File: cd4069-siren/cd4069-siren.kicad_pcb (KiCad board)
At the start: 2 copper layers, 15 parts, among them U1 4069

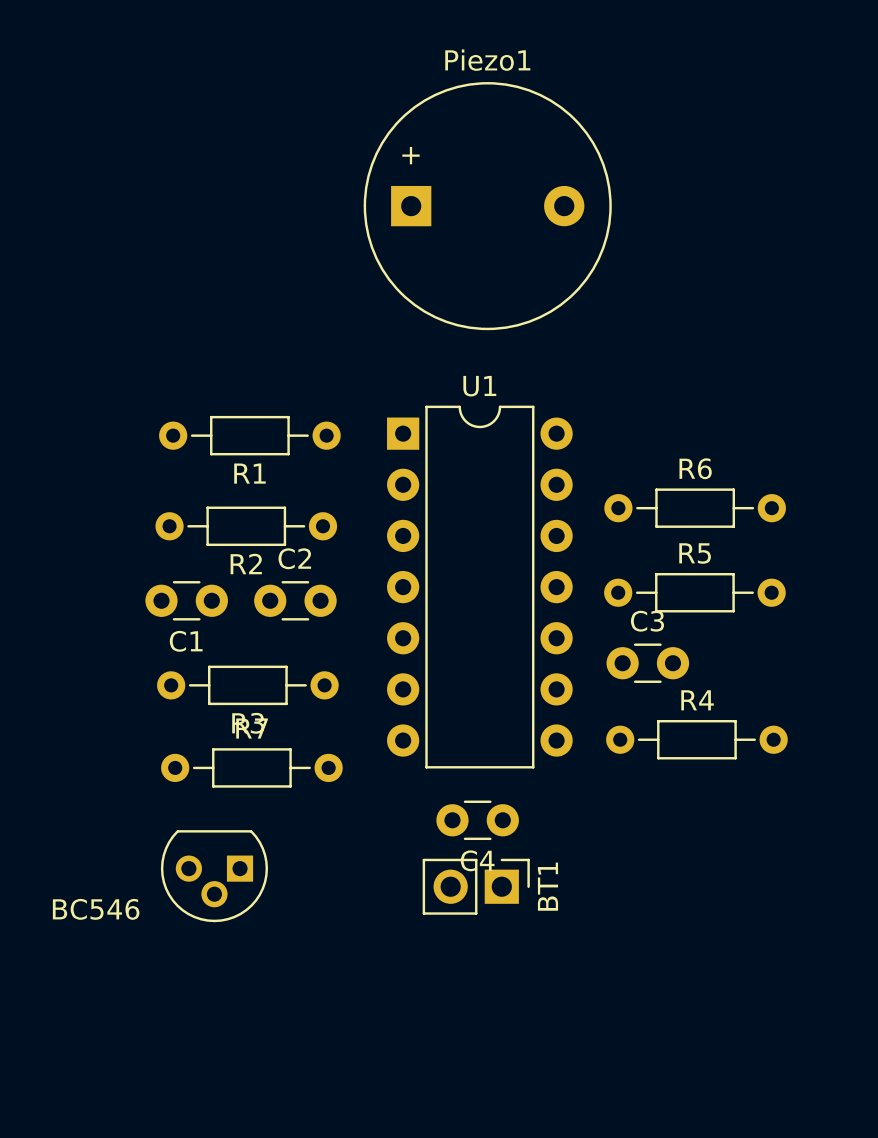
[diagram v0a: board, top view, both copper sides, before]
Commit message: project 7 / cd4069 siren / changed edge cuts, improved tracks, added logo
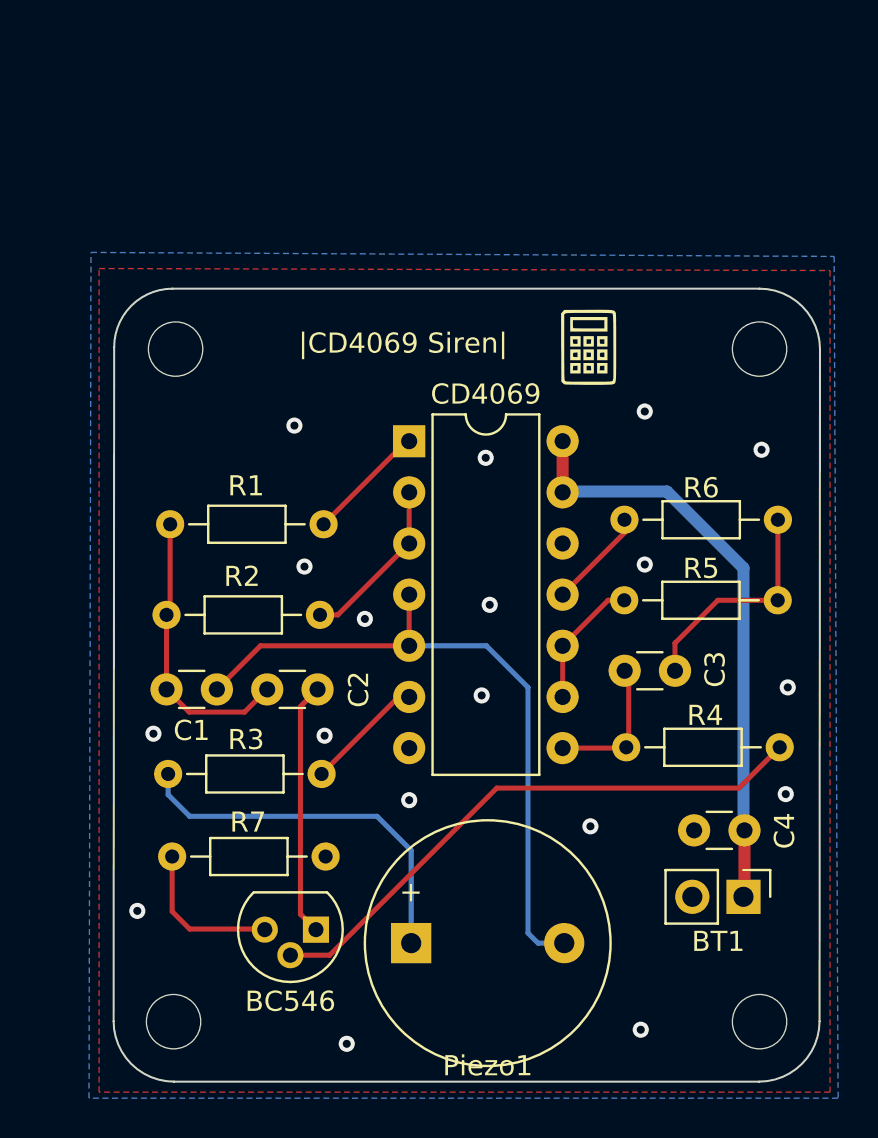
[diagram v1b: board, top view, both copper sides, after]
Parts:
- added G***: LOGO, Graphics:pcbLogo_4mmx4mm, F.Cu at (112.5, 50.3)
- added G***: LOGO, Graphics:pcbLogo_30mmx30mm, B.Cu at (105.9, 68.2)
- added REF**: MountingHole_2.7mm, MountingHole:MountingHole_2.7mm, F.Cu at (121.0, 50.4)
- added REF**: MountingHole_2.7mm, MountingHole:MountingHole_2.7mm, F.Cu at (121.0, 83.8)
- added REF**: MountingHole_2.7mm, MountingHole:MountingHole_2.7mm, F.Cu at (92.0, 50.4)
- added REF**: MountingHole_2.7mm, MountingHole:MountingHole_2.7mm, F.Cu at (91.9, 83.8)
- moved Piezo1 36.6 mm to (103.7, 79.9)
- moved BT1 12.0 mm to (120.2, 77.6)
- moved C4 12.0 mm to (120.2, 74.3)
- moved BC546 4.84 mm to (99.0, 79.2)
- moved C1 4.41 mm to (94.0, 67.3)
- moved R3 4.40 mm to (99.2, 71.5)
- moved C2 4.40 mm to (96.5, 67.3)
- moved R1 4.40 mm to (99.3, 59.1)
- moved R2 4.40 mm to (99.2, 63.6)
- moved R7 4.40 mm to (91.8, 75.6)
- moved R6 0.65 mm to (114.3, 58.9)
- moved CD4069 0.48 mm to (103.6, 55.0)
- moved R4 0.48 mm to (114.4, 70.2)
- moved R5 0.48 mm to (114.3, 62.9)
- moved C3 0.39 mm to (114.3, 66.4)
- renumbered U1 to CD4069
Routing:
- net /I0: track 0.00 -> 33.9 mm
- net +6V: track 0.00 -> 29.5 mm
- net Net-(BC546-B): track 0.00 -> 28.6 mm
- net Net-(Piezo1-Pad1): track 0.00 -> 18.8 mm
- net Net-(C1-Pad2): track 0.00 -> 14.2 mm
- net /I1: track 0.00 -> 12.6 mm
- net Net-(C3-Pad2): track 0.00 -> 11.6 mm
- net Net-(R2-Pad1): track 0.00 -> 8.44 mm
- net Net-(BC546-E): track 0.00 -> 7.70 mm
- net Net-(C3-Pad1): track 0.00 -> 7.11 mm
- net Net-(R5-Pad1): track 0.00 -> 6.54 mm
- net Net-(R3-Pad1): track 0.00 -> 6.22 mm
- net Net-(R1-Pad1): track 0.00 -> 5.96 mm
- net Net-(R6-Pad1): track 0.00 -> 4.99 mm
- net GND: vias 0 -> 18
- added copper zone on B.Cu, net GND
- added copper zone on F.Cu, net GND
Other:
- board outline added: 35.1 x 39.4 mm
- board text added: "|CD4069 Siren|"
